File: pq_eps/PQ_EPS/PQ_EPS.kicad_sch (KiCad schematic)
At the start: 79 parts, among them IC1 SDA, IC2 ISL9120IRTNZ, J1 SLW-110-01-T-S, J2 SLW-110-01-T-S, J3 SLW-110-01-T-S, J4 SLW-110-01-T-S, Q1 SIR424DP-T1-GE3, U1 SPV1040TTR, U2 SPV1040TTR, U3 SPV1040TTR, U4 LTC4040EUFD#PBF

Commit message: Revised schematic 25 jan
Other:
- note added: "Lateral Pins"
- note added: "MOUNTING HOLES"
- moved on the sheet: C1, C2, C3, C4, C5, CF1, CF2, CF3, CIN1, CIN2, CIN3, CINSNS1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

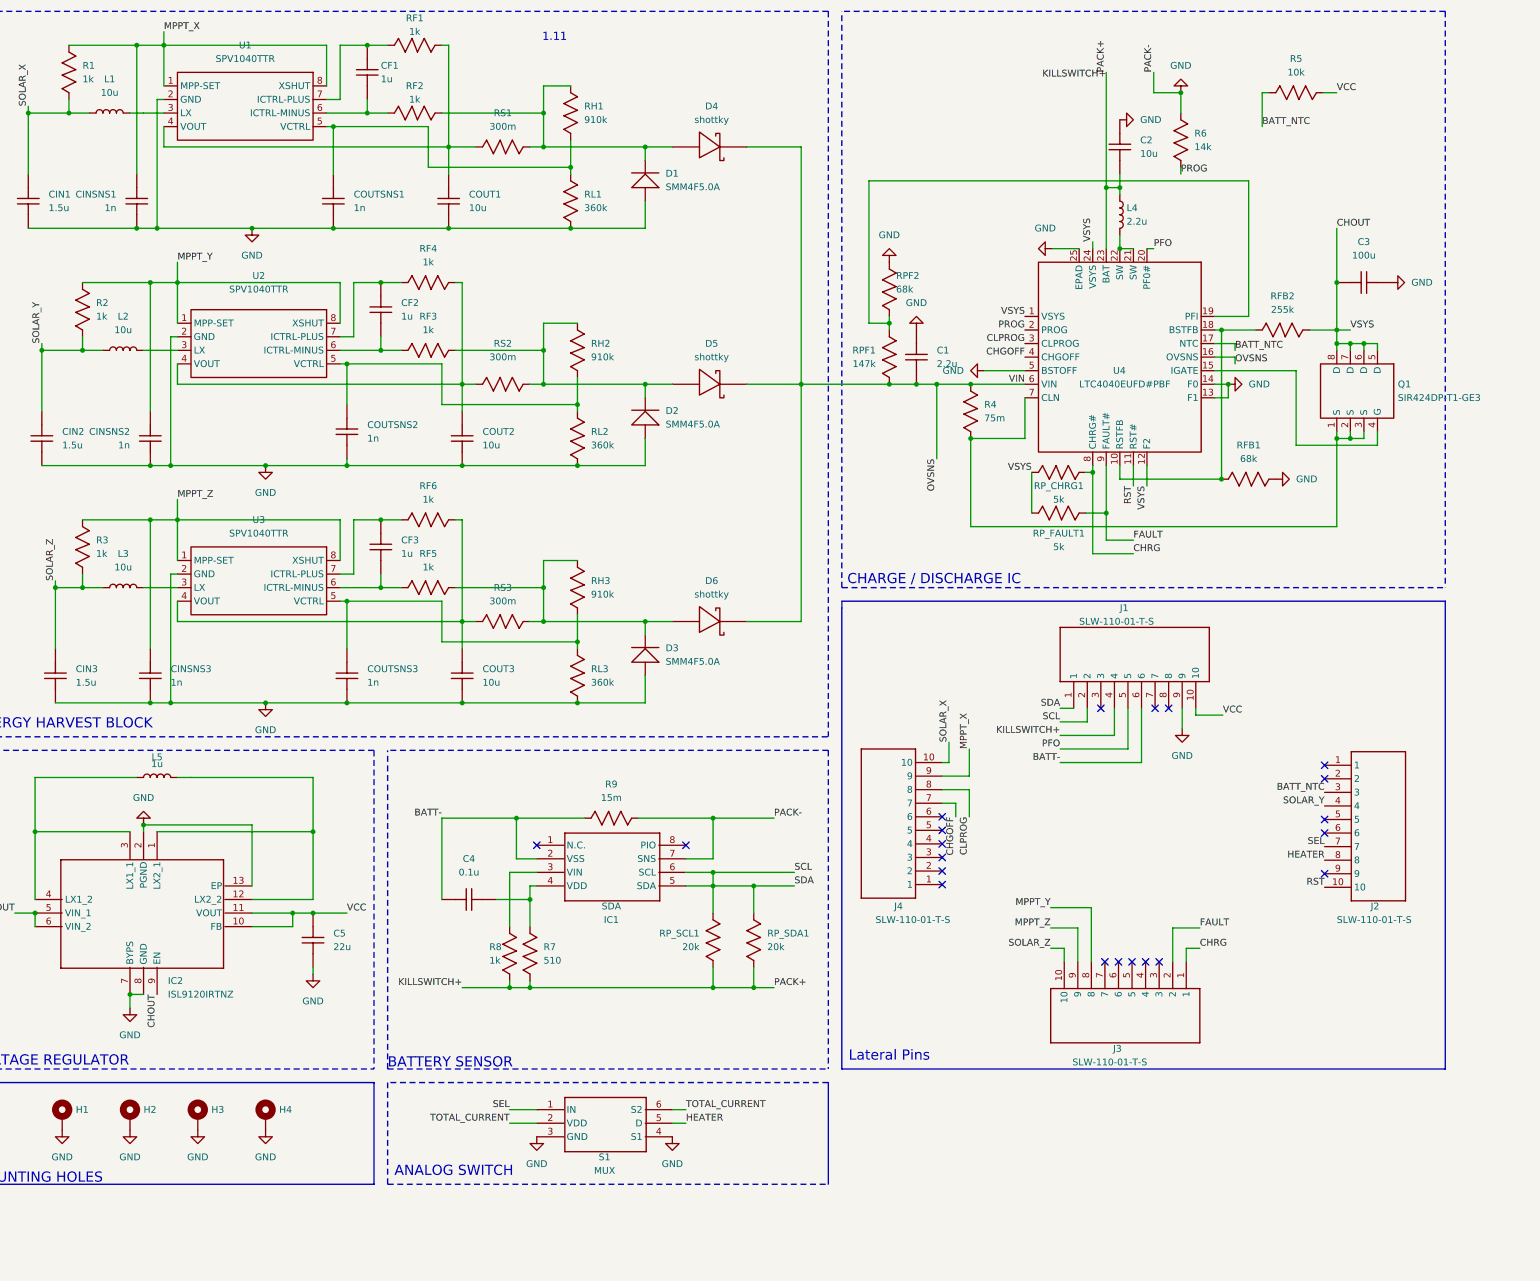
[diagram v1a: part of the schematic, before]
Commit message: EPS LTC 4040 correction and layout revamp
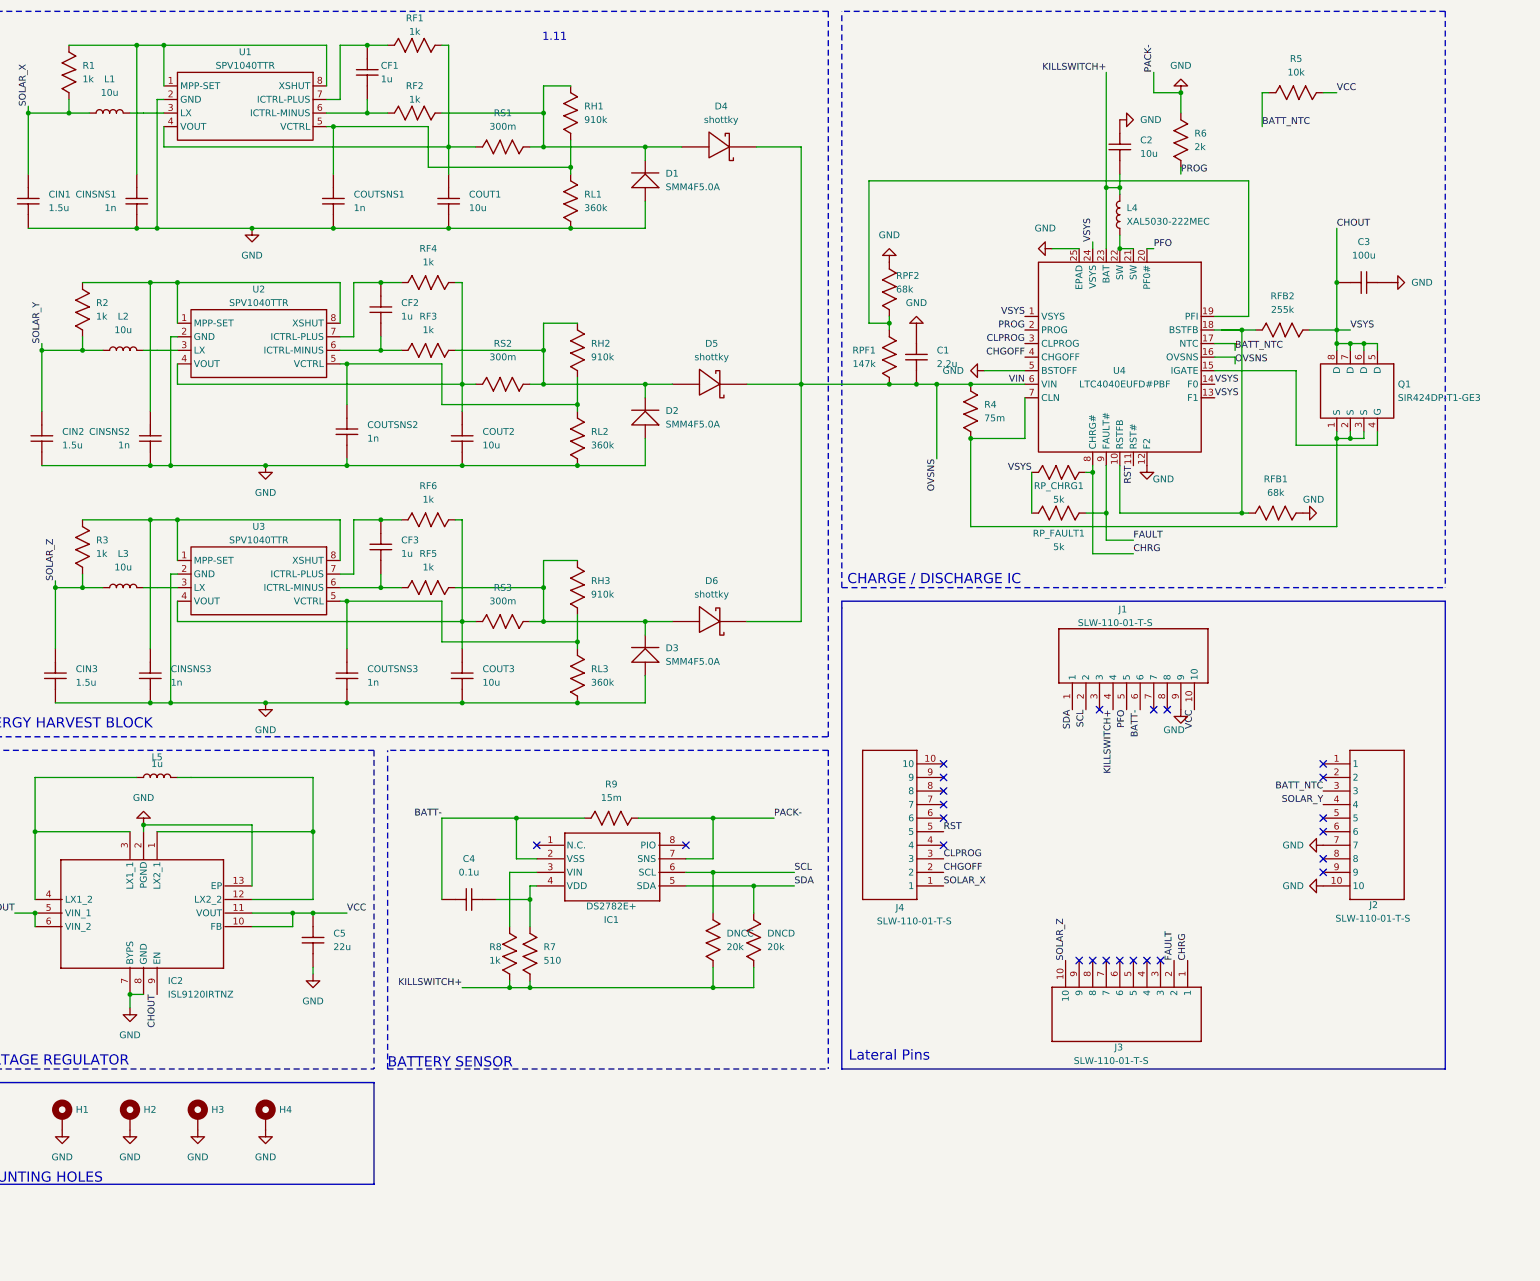
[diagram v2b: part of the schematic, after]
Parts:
- removed S1: MUX, SOT65P210X110-6N, symbol PCB-EPS-altium-import:0_MUX
- C1, CF1, CF2, CF3, CIN1, CIN2, CIN3, CINSNS1, CINSNS2, CINSNS3, COUTSNS1, COUTSNS2, COUTSNS3: footprint C0402 -> Capacitor_SMD:C_0603_1608Metric
- C2, C4, C5, COUT1, COUT2, COUT3: footprint C0603 -> Capacitor_SMD:C_0603_1608Metric
- C3: footprint C1206 -> Capacitor_SMD:C_1206_3216Metric
- D1, D2, D3: footprint DIO_SMM4F5.0A-TR -> SamacSys_Parts:SMM4F15ATR
- D4, D5, D6: footprint SOD-128_L3.7-W2.5-LS4.7-FD -> Diode_SMD:D_SOD-128
- DNCC: renamed from RP_SCL1; footprint R0603 -> Resistor_SMD:R_0603_1608Metric
- DNCD: renamed from RP_SDA1; footprint R0603 -> Resistor_SMD:R_0603_1608Metric
- IC1: value SDA -> DS2782E+; footprint SOP65P640X110-8N -> Package_SO:TSSOP-8_4.4x3mm_P0.65mm
- IC2: footprint QFN50P300X300X75-13N -> SamacSys_Parts:QFN50P300X300X75-13N-D
- J1, J2, J3, J4: footprint SLW-110-01-X-S -> NSL_Connectors:SLW-110-01-X-S
- L1, L2, L3, L5: footprint L0806 -> Inductor_SMD:L_0805_2012Metric
- L4: value 2.2u -> XAL5030-222MEC; footprint L_COILCRAFT_XAL5030 -> SamacSys_Parts:XAL5030222MEC; BOM_LINK https://www.mouser.es/ProductDetail/Coilcraft/XAL5030-222ME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 -> (none); BOM_MANUFACTURER Coilcraft -> (none); BOM_MANUFACTURER PART XAL5030-222MEC -> (none); BOM_SUPPLIER Mouser -> (none); BOM_SUPPLIER PART 994-XAL5030-222MEC -> (none); CONTRIBUTOR LCEDA_Lib -> (none); Height (none) -> 3.1; Manufacturer_Name (none) -> COILCRAFT; Manufacturer_Part_Number (none) -> XAL5030-222MEC; Mouser Part Number (none) -> 994-XAL5030-222MEC; Mouser Price/Stock (none) -> https://www.mouser.co.uk/ProductDetail/Coilcraft/XAL5030-22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; NAMEALIAS Value(H) -> (none); SPICEPRE L -> (none); SPICESYMBOLNAME L0603_US -> (none)
- Q1: footprint POWERPAK-SO-8_L6.2-W5.2-P1.27-BL-EP -> Package_SO:SO-8_5.3x6.2mm_P1.27mm
- R1, R2, R3: footprint R0805 -> Resistor_SMD:R_0603_1608Metric
- R4, RP_CHRG1, RP_FAULT1: footprint R0805 -> Resistor_SMD:R_0805_2012Metric
- R5, R8, RF1, RF2, RF3, RF4, RF5, RF6, RFB1, RPF2: footprint R0402 -> Resistor_SMD:R_0603_1608Metric
- R6: value 14k -> 2k; footprint R0603 -> Resistor_SMD:R_0603_1608Metric
- R7, R9, RH1, RH2, RH3, RL1, RL2, RL3, RPF1, RS1, RS2, RS3: footprint R0603 -> Resistor_SMD:R_0603_1608Metric
- RFB2: footprint R0402 -> Resistor_SMD:R_0402_1005Metric
- U1, U2, U3: footprint TSSOP-8_L4.4-W3.0-P0.65-LS6.4-BL -> Package_SO:TSSOP-8_4.4x3mm_P0.65mm
- U4: footprint VQFN-24_L5.0-W4.0-P0.50-BL-EP -> Package_DFN_QFN:QFN-24-1EP_4x5mm_P0.5mm_EP2.65x3.65mm
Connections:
- net SEL is gone; now on net GND: J2.7
- net CHGOFF: now also J4.2; no longer J4.7
- net CHOUT: now also U4.13 (F1), U4.14 (F0); no longer U4.12 (F2)
- net CLPROG: now also J4.3; no longer J4.8
- net GND: now also J2.10, U4.12 (F2); no longer U4.13 (F1), U4.14 (F0)
- net KILLSWITCH+: now also L4.2; no longer L4.1
- net RST: now also J4.5; no longer J2.10
- net SCL: no longer DNCD.2, IC1.5 (SDA), J1.1
- net SOLAR_X: now also J4.1, L1.2; no longer J4.10, L1.1
- net at U1.3 (LX): now also L1.1; no longer L1.2
- net at U4.21 (SW), U4.22 (SW): now also L4.1; no longer L4.2
- net HEATER: no longer names the net of J2.8
- net MPPT_X: no longer names the net of CINSNS1.2, R1.2, U1.1 (MPP-SET), U1.8 (XSHUT)
- net MPPT_X: no longer J4.9
- net MPPT_Y: no longer names the net of CINSNS2.2, R2.2, U2.1 (MPP-SET), U2.8 (XSHUT)
- net MPPT_Y: no longer J3.8
- net MPPT_Z: no longer names the net of CINSNS3.2, R3.2, U3.1 (MPP-SET), U3.8 (XSHUT)
- net MPPT_Z: no longer J3.9
- new net SDA: DNCD.2, IC1.5 (SDA), J1.1
- no-connect marks 21 -> 24
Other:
- note removed: "ANALOG SWITCH"
- moved on the sheet: D4, L1, RFB1

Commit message: EPS board revised and Guillem approved
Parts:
- Q1: footprint Package_SO:SO-8_5.3x6.2mm_P1.27mm -> Package_SO:PowerPAK_SO-8_Single
- renumbered DNCC to DNC1, DNCD to DNC2
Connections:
- net CHOUT: no longer Q1.6 (D), Q1.7 (D), Q1.8 (D)
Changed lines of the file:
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@@
   (junction (at 101.6 33.02) (diameter 0) (color 0 0 0 0)
   )
-  (junction (at 308.61 86.36) (diameter 0) (color 0 0 0 0)
-  )
   (junction (at 242.57 85.09) (diameter 0) (color 0 0 0 0)
   )
@@
   (junction (at 82.55 195.58) (diameter 0) (color 0 0 0 0)
   )
+  (junction (at 308.61 86.36) (diameter 0) (color 0 0 0 0)
+  )
   (junction (at 162.56 156.21) (diameter 0) (color 0 0 0 0)
   )
@@
   (junction (at 147.32 134.62) (diameter 0) (color 0 0 0 0)
   )
-  (junction (at 328.93 88.9) (diameter 0) (color 0 0 0 0)
-  )
   (junction (at 104.14 111.76) (diameter 0) (color 0 0 0 0)
   )
@@
   (junction (at 106.68 33.02) (diameter 0) (color 0 0 0 0)
   )
-  (junction (at 326.39 88.9) (diameter 0) (color 0 0 0 0)
-  )
-  (junction (at 331.47 88.9) (diameter 0) (color 0 0 0 0)
-  )
   (junction (at 326.39 106.68) (diameter 0) (color 0 0 0 0)
   )
@@
     (stroke (width 0.254) (type default) (color 0 0 0 0))
   )
+  (wire (pts (xy 303.53 86.36) (xy 308.61 86.36))
+    (stroke (width 0) (type default) (color 0 0 0 0))
+  )
   (wire (pts (xy 177.8 45.72) (xy 177.8 52.07))
     (stroke (width 0.254) (type default) (color 0 0 0 0))
@@
     (stroke (width 0.254) (type default) (color 0 0 0 0))
   )
-  (wire (pts (xy 334.01 88.9) (xy 331.47 88.9))
-    (stroke (width 0.254) (type default) (color 0 0 0 0))
-  )
   (wire (pts (xy 175.26 193.04) (xy 175.26 198.12))
     (stroke (width 0.254) (type default) (color 0 0 0 0))
@@
     (stroke (width 0.254) (type default) (color 0 0 0 0))
   )
-  (wire (pts (xy 328.93 88.9) (xy 326.39 88.9))
-    (stroke (width 0.254) (type default) (color 0 0 0 0))
-  )
   (wire (pts (xy 177.8 96.52) (xy 196.85 96.52))
     (stroke (width 0.254) (type default) (color 0 0 0 0))
@@
     (stroke (width 0.254) (type default) (color 0 0 0 0))
   )
-  (wire (pts (xy 328.93 90.17) (xy 328.93 88.9))
-    (stroke (width 0.254) (type default) (color 0 0 0 0))
-  )
   (wire (pts (xy 326.39 123.19) (xy 257.81 123.19))
     (stroke (width 0.254) (type default) (color 0 0 0 0))
@@
     (stroke (width 0.254) (type default) (color 0 0 0 0))
   )
-  (wire (pts (xy 331.47 88.9) (xy 328.93 88.9))
+  (wire (pts (xy 326.39 88.9) (xy 334.01 88.9))
     (stroke (width 0.254) (type default) (color 0 0 0 0))
   )
@@
     (stroke (width 0.254) (type default) (color 0 0 0 0))
   )
-  (wire (pts (xy 308.61 86.36) (xy 304.8 86.36))
-    (stroke (width 0) (type default) (color 0 0 0 0))
-  )
   (wire (pts (xy 307.34 88.9) (xy 303.53 88.9))
     (stroke (width 0.254) (type default) (color 0 0 0 0))
@@
     (stroke (width 0.254) (type default) (color 0 0 0 0))
   )
-  (wire (pts (xy 331.47 90.17) (xy 331.47 88.9))
-    (stroke (width 0.254) (type default) (color 0 0 0 0))
-  )
   (polyline (pts (xy 231.14 26.67) (xy 231.14 162.56))
     (stroke (width 0.254) (type dash) (color 0 0 0 0))
@@
     (stroke (width 0.254) (type default) (color 0 0 0 0))
   )
-  (wire (pts (xy 326.39 90.17) (xy 326.39 88.9))
-    (stroke (width 0.254) (type default) (color 0 0 0 0))
-  )
   (wire (pts (xy 162.56 77.47) (xy 162.56 96.52))
     (stroke (width 0.254) (type default) (color 0 0 0 0))
@@
     (stroke (width 0.254) (type default) (color 0 0 0 0))
   )
-  (wire (pts (xy 303.53 86.36) (xy 308.61 86.36))
-    (stroke (width 0.254) (type default) (color 0 0 0 0))
-  )
   (wire (pts (xy 109.22 90.17) (xy 105.41 90.17))
     (stroke (width 0.254) (type default) (color 0 0 0 0))
@@
   (symbol (lib_id "PCB-EPS-altium-import:1_20k") (at 217.17 200.66 0) (unit 1)
     (in_bom yes) (on_board yes) (fields_autoplaced)
-    (property "Reference" "DNCD" (id 0) (at 219.71 199.3899 0)
+    (property "Reference" "DNC2" (id 0) (at 219.71 199.3899 0)
       (effects (font (size 1.27 1.27)) (justify left))
     )
@@
       (effects (font (size 1.27 1.27)) (justify left))
     )
-    (property "Footprint" "Package_SO:SO-8_5.3x6.2mm_P1.27mm" (id 2) (at 330.2 97.79 0)
+    (property "Footprint" "Package_SO:PowerPAK_SO-8_Single" (id 2) (at 330.2 97.79 0)
       (effects (font (size 1.27 1.27)) hide)
     )
@@
     (pin "4")
     (pin "5")
-    (pin "6")
-    (pin "7")
-    (pin "8")
   )
   (symbol (lib_id "power:GND") (at 242.57 73.66 180) (unit 1)
@@
   (symbol (lib_id "PCB-EPS-altium-import:1_20k") (at 209.55 200.66 0) (unit 1)
     (in_bom yes) (on_board yes) (fields_autoplaced)
-    (property "Reference" "DNCC" (id 0) (at 212.09 199.3899 0)
+    (property "Reference" "DNC1" (id 0) (at 212.09 199.3899 0)
       (effects (font (size 1.27 1.27)) (justify left))
     )
@@
     )
     (path "/da46df59-4c28-48ab-b37e-062ef5aab7b8"
-      (reference "DNCC") (unit 1) (value "20k") (footprint "Resistor_SMD:R_0603_1608Metric")
+      (reference "DNC1") (unit 1) (value "20k") (footprint "Resistor_SMD:R_0603_1608Metric")
     )
     (path "/82964add-0911-40f2-a916-19703ce2f759"
-      (reference "DNCD") (unit 1) (value "20k") (footprint "Resistor_SMD:R_0603_1608Metric")
+      (reference "DNC2") (unit 1) (value "20k") (footprint "Resistor_SMD:R_0603_1608Metric")
     )
     (path "/12c30cb3-102e-4571-8fff-4d01e9ce650a"
@@
     )
     (path "/bf2acc0d-fd2e-4c93-9b25-264078ec9e9e"
-      (reference "Q1") (unit 1) (value "SIR424DP-T1-GE3") (footprint "Package_SO:SO-8_5.3x6.2mm_P1.27mm")
+      (reference "Q1") (unit 1) (value "SIR424DP-T1-GE3") (footprint "Package_SO:PowerPAK_SO-8_Single")
     )
     (path "/5c42fe84-2a28-4171-90e3-5a8274ddb455"

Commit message: Functional revision and finishing touches part I
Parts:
- removed D1, D2, D3: SMM4F5.0A, SamacSys_Parts:SMM4F15ATR, symbol PCB-EPS-altium-import:1_SMM4F5.0A
- added Annotation1: Silkscreen_Annotation, symbols-nsl:Bridgemaker, symbol symbols-nsl:Silkscreen_Annotation
- added Annotation2: Silkscreen_Annotation, symbols-nsl:NakNak, symbol symbols-nsl:Silkscreen_Annotation
- added D1, D2, D3: SMM4F, passive-nsl:SMM4F15ATR, symbol passive-nsl:SMM4F
- IC2: footprint SamacSys_Parts:QFN50P300X300X75-13N-D -> Package_DFN_QFN:QFN-12-1EP_3x3mm_P0.5mm_EP1.6x1.6mm
- J1: footprint NSL_Connectors:SLW-110-01-X-S -> connector-nsl:SLW-110-01; symbol PCB-EPS-altium-import:1_SLW-110-01-T-S -> connector-nsl:SLW-110-01
- J2: footprint NSL_Connectors:SLW-110-01-X-S -> connector-nsl:SLW-110-01; symbol PCB-EPS-altium-import:0_SLW-110-01-T-S -> connector-nsl:SLW-110-01
- J3: footprint NSL_Connectors:SLW-110-01-X-S -> connector-nsl:SLW-110-01; symbol PCB-EPS-altium-import:3_SLW-110-01-T-S -> connector-nsl:SLW-110-01
- J4: footprint NSL_Connectors:SLW-110-01-X-S -> connector-nsl:SLW-110-01; symbol PCB-EPS-altium-import:2_SLW-110-01-T-S -> connector-nsl:SLW-110-01
- L4: footprint SamacSys_Parts:XAL5030222MEC -> passive-nsl:XAL5030222MEC
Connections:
- net GND: now also D1.2, D2.2, D3.2
- net at D5.2, RF3.2, RH2.2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: now also D2.1
- net at D6.2, RF5.2, RH3.2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: now also D3.1
- net at D4.2, RF2.2, RH1.2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: now also D1.1
